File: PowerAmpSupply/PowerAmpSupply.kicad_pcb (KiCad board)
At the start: 4 copper layers, 80.5 x 40 mm, 89 parts, among them J1 VIN_BRIDGE, J2 VIN_BRIDGE, J3 GND_BRIDGE, J4 GND_BRIDGE, J5 VOUT, J6 VIN, J7 VTRK_EXT, M1 12V 6Vstart <100mA, Q1 EPC2306, Q2 PNP, Q3 EPC2306, Q4 PNP, U1 LM5123-Q1, U2 NCP51460, U3 AP2202-ADJ, U4 TPSM365R3

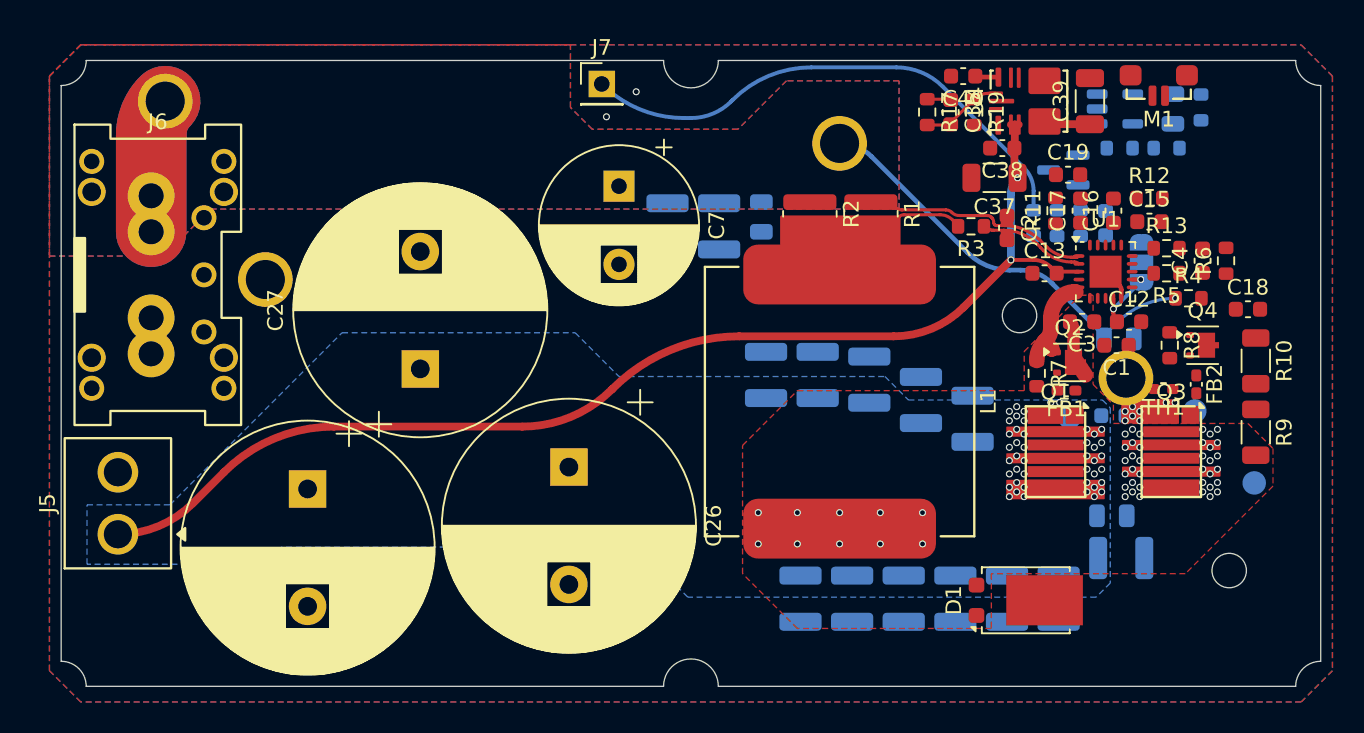
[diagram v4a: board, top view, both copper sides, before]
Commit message: PowerAmp+Supply additions
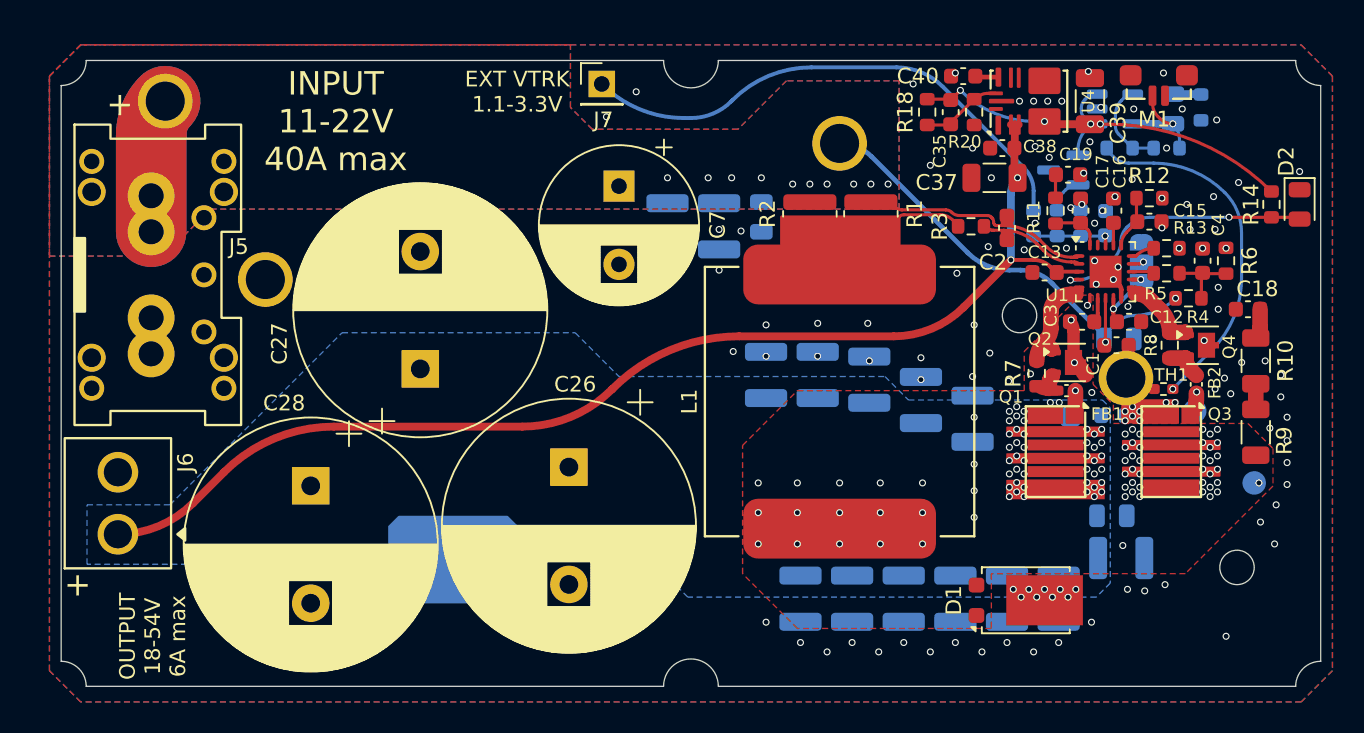
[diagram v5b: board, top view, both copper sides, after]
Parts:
- removed the REF** at (171.0, 96.3)
- removed the REF** at (184.4, 112.6)
- added D2: PGOOD, LED_SMD:LED_0805_2012Metric, F.Cu at (188.9, 89.2)
- added Logo: BW_Logo_7.5x4.8mm, BW_Logo:BW_Logo_7.5x4.8mm, B.Cu at (134.8, 111.9)
- added R14: 4.7kΩ, Resistor_SMD:R_0603_1608Metric, F.Cu at (187.1, 89.2)
- added REF**: Heatspreader_PowerAmpSupply, BW_PassiveMechanical:Heatspreader_PowerAmpSupply, F.Cu at (177.9, 104.3)
- moved C25 25.5 mm to (177.5, 111.8), turned to 0 degrees
- moved C24 23.5 mm to (154.8, 100.1), turned to 90 degrees
- moved C23 22.7 mm to (158.1, 100.1), turned to 90 degrees
- moved C32 15.3 mm to (163.6, 114.4), turned to -90 degrees
- moved C29 3.30 mm to (173.5, 114.4)
- moved C31 3.30 mm to (166.9, 114.4)
- moved C30 3.30 mm to (170.2, 114.4)
- moved C28 0.28 mm to (125.7, 107.2)
- moved TP2 0.05 mm to (174.2, 102.8)
- renumbered REF** to HS, J6 to J5, J5 to J6, R14 to R15, R15 to R16, R16 to R17, R17 to R18, R18 to R19, R19 to R20, R20 to R21, R21 to R22
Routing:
- net +12V: track 4.46 -> 29.6 mm, vias 0 -> 4
- net Net-(R21-Pad2): track 0.00 -> 22.7 mm, vias 0 -> 1
- net /PGOOD: track 0.00 -> 17.2 mm, vias 0 -> 2
- net Net-(M1-+): track 0.00 -> 6.73 mm, vias 0 -> 1
- net Net-(U3-ADJ): track 0.00 -> 5.76 mm
- net Net-(Q4-B): track 0.00 -> 5.49 mm
- net /VTRK: track 0.00 -> 5.26 mm, vias 0 -> 1
- net /EN: track 0.00 -> 4.64 mm
- net Net-(U1-VREF/RANGE): track 0.00 -> 3.38 mm
- net Net-(Q1-G): track 0.00 -> 3.35 mm, vias 0 -> 1
- net Net-(U1-COMP): track 0.00 -> 3.28 mm
- net /VIN: track 76.3 -> 79.3 mm, vias 1 -> 12
- net Net-(Q3-G): track 0.00 -> 2.71 mm, vias 0 -> 1
- net Net-(Q4-E): track 0.00 -> 2.69 mm
- net Net-(Q2-E): track 0.00 -> 2.62 mm
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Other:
- board text added: "+"
- board text added: "EXT VTRK 1.1-3.3V"
- board text added: "INPUT 11-22V 40A max"
- board text added: "LO HI VH/CP"
- board text added: "Modular Audio Power Amp Supply"
- board text added: "OUTPUT 18-54V 6A max"

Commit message: PowerAmpSupply final + ICL, PowerAmp final
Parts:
- added C41: 10µF 50V, Capacitor_SMD:C_1206_3216Metric, B.Cu at (129.4, 90.6)
- added C42: 0.1µF, Capacitor_SMD:C_0603_1608Metric, F.Cu at (133.1, 82.9)
- added C43: 1µF 50Vl, Capacitor_SMD:C_0805_2012Metric, B.Cu at (124.8, 87.5)
- added C44: 0.1µF, Capacitor_SMD:C_0603_1608Metric, B.Cu at (126.2, 90.9)
- added C45: 10µF 75V x2, Capacitor_SMD:C_1210_3225Metric, B.Cu at (129.3, 93.4)
- added C46: 4.7µF, Capacitor_SMD:C_0603_1608Metric, B.Cu at (133.6, 86.5)
- added C47: 1µF, Capacitor_SMD:C_0603_1608Metric, F.Cu at (126.6, 83.8)
- added D3: BZT52C10, Diode_SMD:D_SOD-123, F.Cu at (138.4, 86.5)
- added D4: BZT52C10, Diode_SMD:D_SOD-123, B.Cu at (138.2, 88.5)
- added D5: BZT52C12, Diode_SMD:D_SOD-123, F.Cu at (133.6, 86.5)
- added D6: SS0840WS, Diode_SMD:D_SOD-323_HandSoldering, B.Cu at (134.9, 89.6)
- added F1: 6.3A, BW_PassiveMechanical:Fuse_Schurter_MSB, B.Cu at (120.8, 110.5)
- added L2: 100nH, BW_PassiveMechanical:L_Pulse_PG2110HLT, B.Cu at (121.6, 82.9)
- added Q5: SiR500DP, Package_SO:PowerPAK_SO-8_Single, B.Cu at (131.1, 83.0)
- added Q6: CMLDM7002AJ, Package_TO_SOT_SMD:SOT-563, F.Cu at (129.7, 85.0)
- added R23: 100Ω, Resistor_SMD:R_0603_1608Metric, F.Cu at (130.0, 82.9)
- added R24: 330kΩ, Resistor_SMD:R_0603_1608Metric, F.Cu at (135.8, 84.6)
- added R25: 13kΩ, Resistor_SMD:R_0603_1608Metric, B.Cu at (135.9, 85.9)
- added R26: 7.5kΩ, Resistor_SMD:R_0603_1608Metric, B.Cu at (123.0, 87.7)
- added R27: 1MΩ, Resistor_SMD:R_0603_1608Metric, B.Cu at (132.9, 88.9)
- added R28: 22Ω, Resistor_SMD:R_0603_1608Metric, F.Cu at (132.7, 84.5)
- added R29: 2kΩ, Resistor_SMD:R_0603_1608Metric, B.Cu at (124.6, 90.9)
- added R30: 100kΩ, Resistor_SMD:R_0603_1608Metric, F.Cu at (129.5, 87.0)
- added R31: 10kΩ, Resistor_SMD:R_0603_1608Metric, F.Cu at (126.6, 85.3)
- added U5: LTC3290, Package_SO:MSOP-10-1EP_3x3mm_P0.5mm_EP1.68x1.88mm, B.Cu at (129.0, 87.6)
- R14: value 4.7kΩ -> 13.3kΩ
- moved J1 20.4 mm to (136.8, 82.5)
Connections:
- J5 pad 2: /VIN -> /Inrush Limit/IN
- J6 pad 1: /VOUT -> /VOUT_FUSED
- R14 pad 1: +12V -> /VOUT_FUSED
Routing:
- net /VOUT_FUSED: track 0.00 -> 89.8 mm, vias 0 -> 2
- net /VIN: track 79.3 -> 45.0 mm
- net /Inrush Limit/IN: track 0.00 -> 33.3 mm, vias 0 -> 1
- net /Inrush Limit/EN: track 0.00 -> 16.0 mm, vias 0 -> 1
- net +12V: track 29.6 -> 17.5 mm
- net /VOUT: track 76.3 -> 66.6 mm
- net Net-(D5-K): track 0.00 -> 8.55 mm, vias 0 -> 1
- net Net-(D6-A): track 0.00 -> 6.69 mm
- net Net-(Q5-D): track 0.00 -> 6.31 mm, vias 0 -> 12
- net Net-(D4-K): track 0.00 -> 5.84 mm
- net Net-(Q6A-D): track 0.00 -> 3.59 mm
- net GND: track 3.12 -> 6.53 mm, vias 124 -> 132
- net Net-(U5-C+): track 0.00 -> 2.34 mm
- net Net-(U5-C-): track 0.00 -> 2.19 mm
- net Net-(U5-VSET): track 0.00 -> 1.76 mm
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- added copper zone on F.Cu, net Net-(Q5-D)
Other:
- board text added: "EXT VTRK"
- board text removed: "EXT VTRK 1.1-3.3V"
